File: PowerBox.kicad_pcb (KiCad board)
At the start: 2 copper layers, 71.1 x 76.2 mm, 7 parts, among them J1 Screw_Terminal_01x16, U1 MP1584EN, U2 MP1584EN, U3 MP1584EN, U4 MP1584EN, U5 MP1584EN, U6 MP1584EN

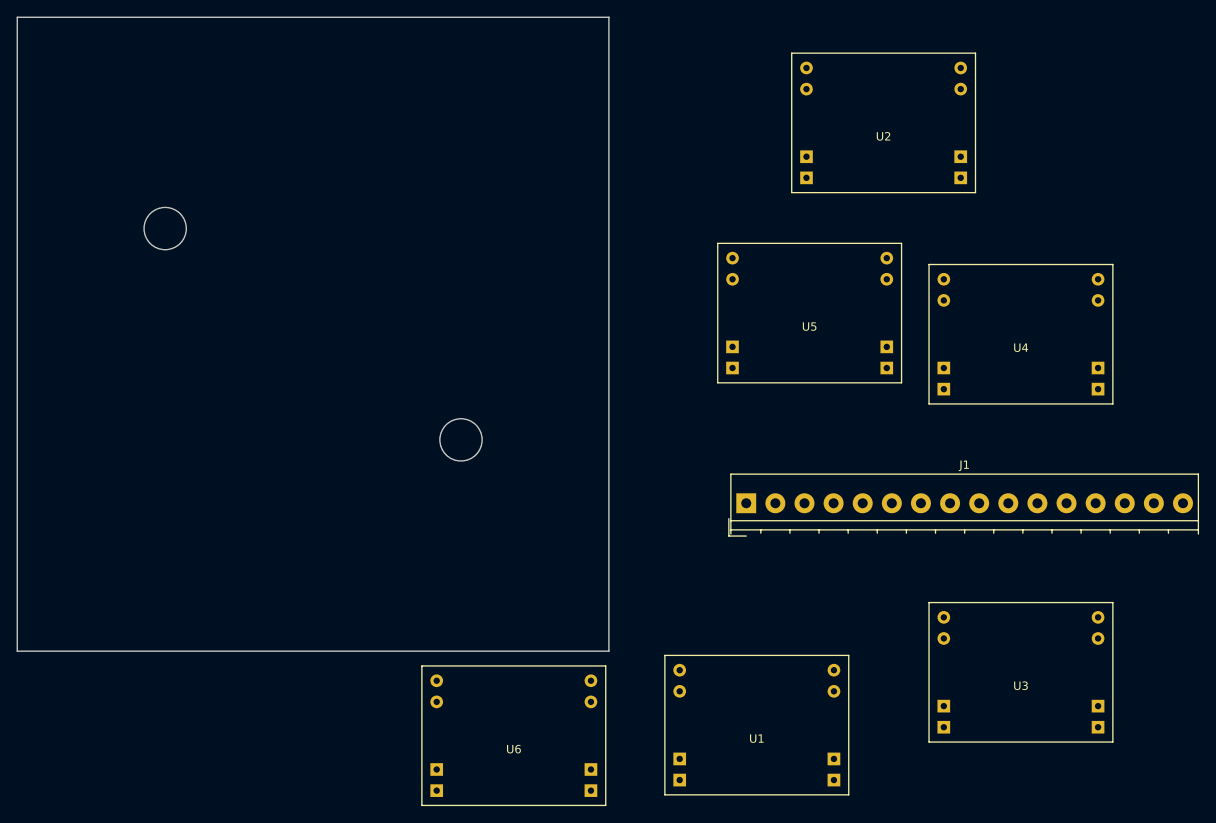
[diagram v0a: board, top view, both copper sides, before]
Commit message: fixed terminal block footprint. layed out tracks for all components.
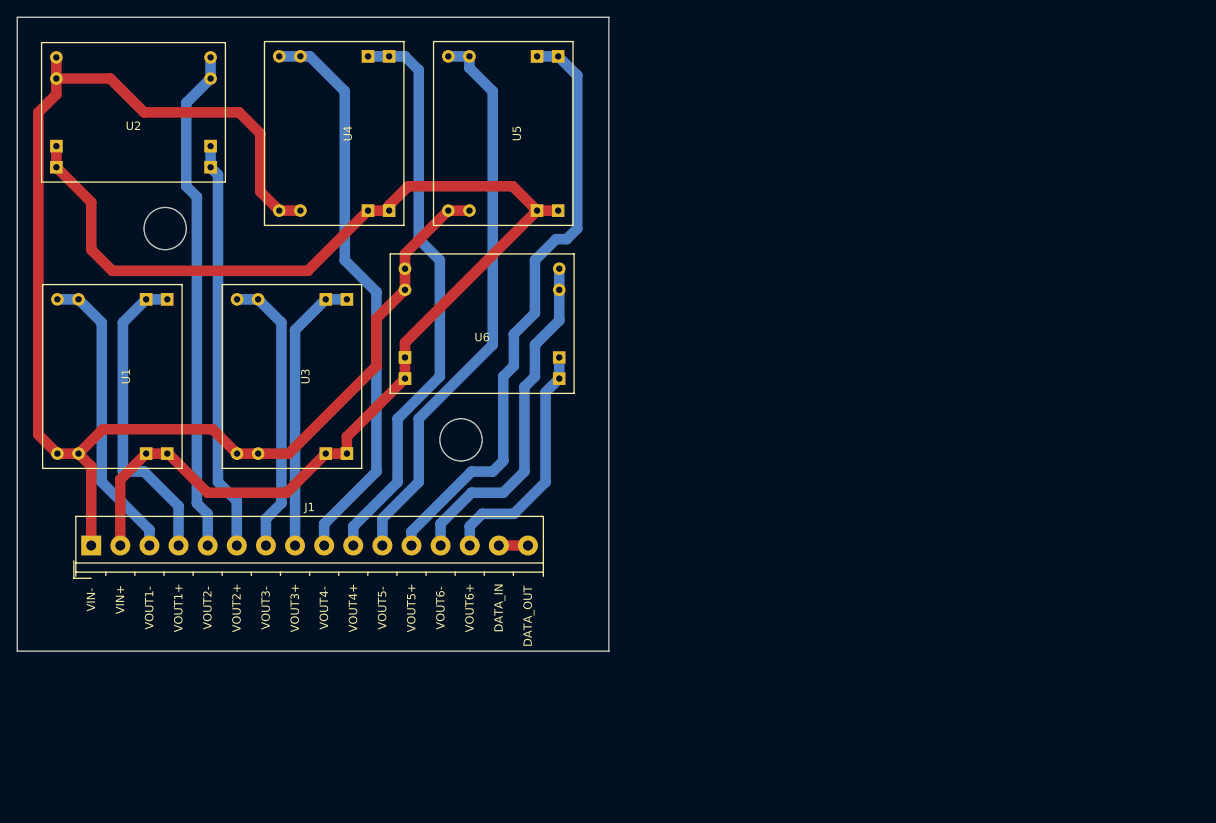
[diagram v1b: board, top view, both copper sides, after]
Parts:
- J1: footprint Connectors_Terminal_Blocks:TerminalBlock_4UCON_19963_16x3.5mm_Straight -> footprints:TerminalBlock_4UCON_19963_16x3.5mm_Straight_MOD
- moved U3 94.6 mm to (134.6, 94.0), turned to 90 degrees
- moved U2 90.2 mm to (115.6, 62.2)
- moved U1 88.1 mm to (113.0, 94.0), turned to 90 degrees
- moved U4 86.0 mm to (139.7, 64.8), turned to 90 degrees
- moved J1 78.9 mm to (110.5, 114.3)
- moved U6 49.7 mm to (157.5, 87.6)
- moved U5 42.7 mm to (160.0, 64.8), turned to 90 degrees
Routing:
- net Net-(J1-Pad1): track 0.00 -> 171.1 mm
- net Net-(J1-Pad2): track 0.00 -> 156.2 mm
- net Net-(J1-Pad12): track 0.00 -> 72.8 mm
- net Net-(J1-Pad10): track 0.00 -> 69.3 mm
- net Net-(J1-Pad9): track 0.00 -> 68.4 mm
- net Net-(J1-Pad11): track 0.00 -> 68.1 mm
- net Net-(J1-Pad5): track 0.00 -> 60.9 mm
- net Net-(J1-Pad6): track 0.00 -> 49.3 mm
- net Net-(J1-Pad13): track 0.00 -> 41.4 mm
- net Net-(J1-Pad4): track 0.00 -> 38.0 mm
- net Net-(J1-Pad3): track 0.00 -> 35.7 mm
- net Net-(J1-Pad7): track 0.00 -> 34.1 mm
- net Net-(J1-Pad8): track 0.00 -> 33.7 mm
- net Net-(J1-Pad14): track 0.00 -> 29.3 mm
- net Net-(J1-Pad15): track 0.00 -> 3.50 mm
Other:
- net class Default: clearance 0.2 -> 0.254; trace_width 0.25 -> 1.27
- rule trace_clearance: 0.2 -> 0.254

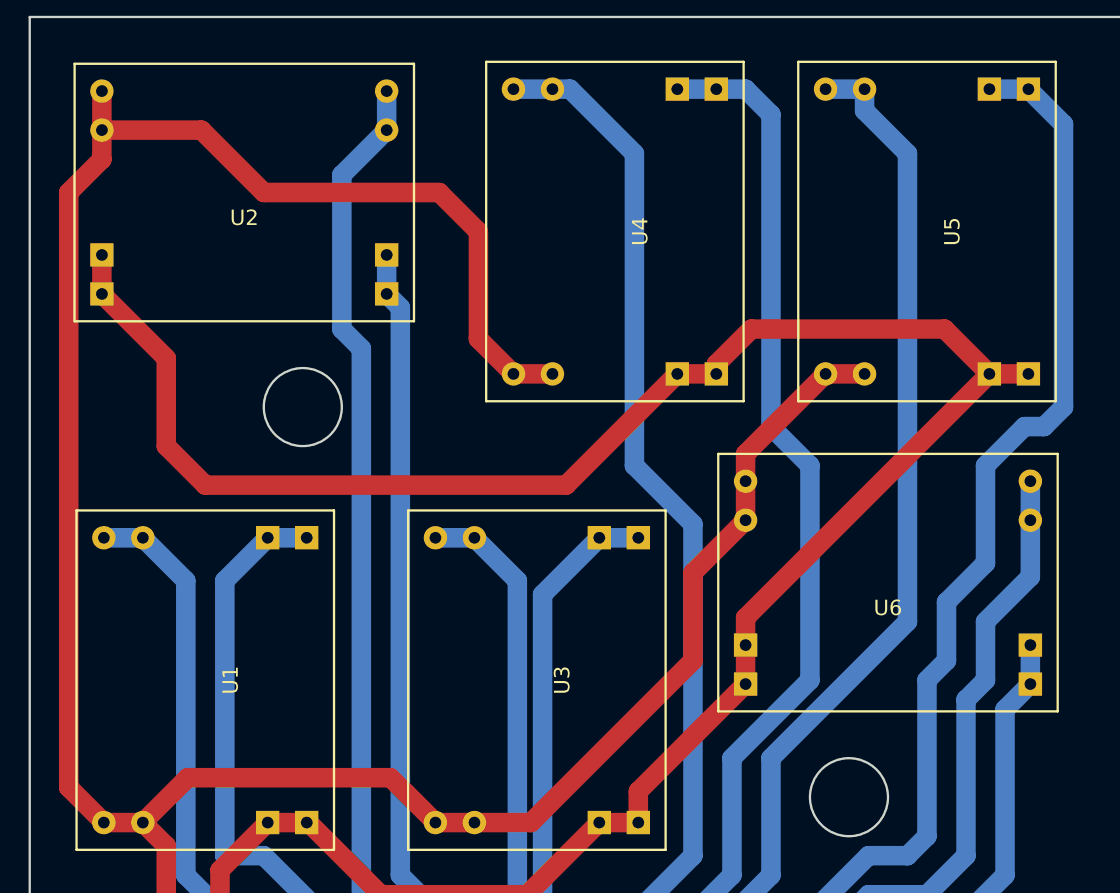
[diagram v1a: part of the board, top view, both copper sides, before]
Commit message: fixed MP1584EN footprint to have text
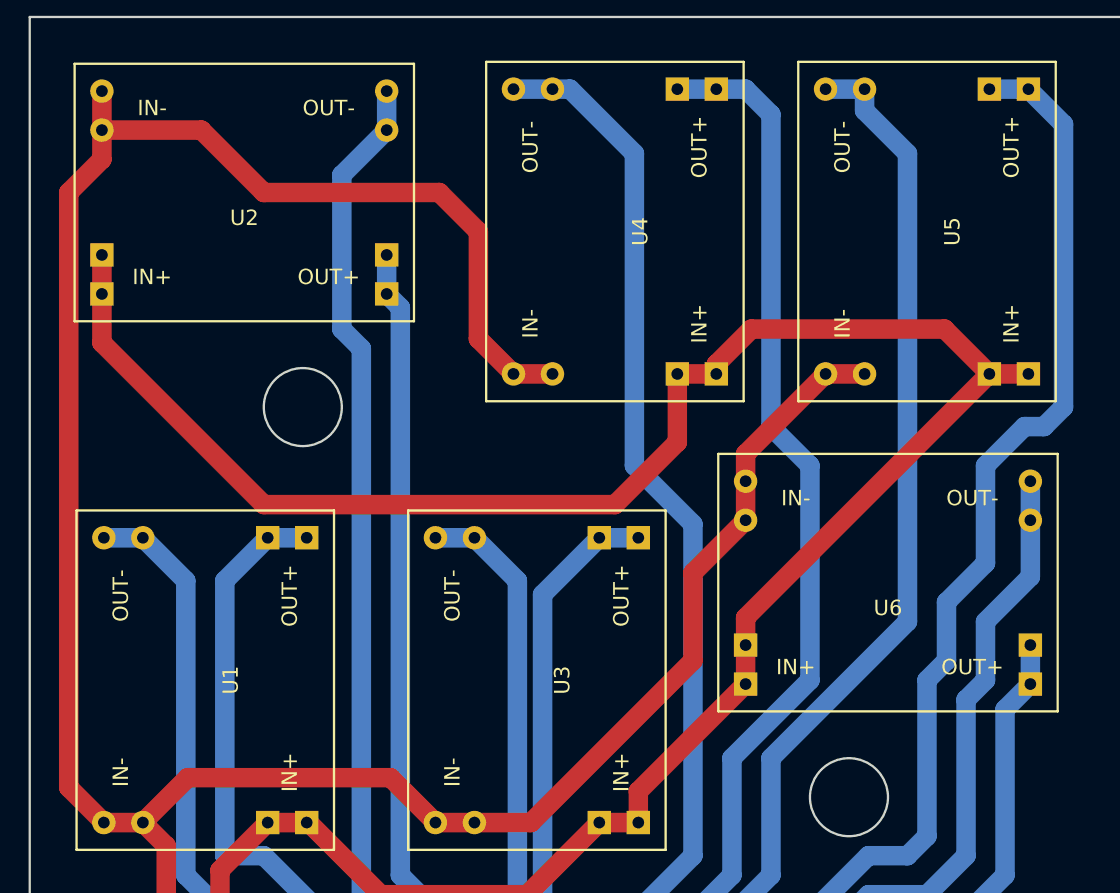
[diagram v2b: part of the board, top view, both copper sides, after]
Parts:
- U1, U2, U3, U4, U5, U6: footprint footprints:MP1584EN -> footprints:MP1584EN_TEXT
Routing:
- net Net-(J1-Pad2): track 156.2 -> 158.4 mm
